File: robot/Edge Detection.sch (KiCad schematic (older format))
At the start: 3 parts

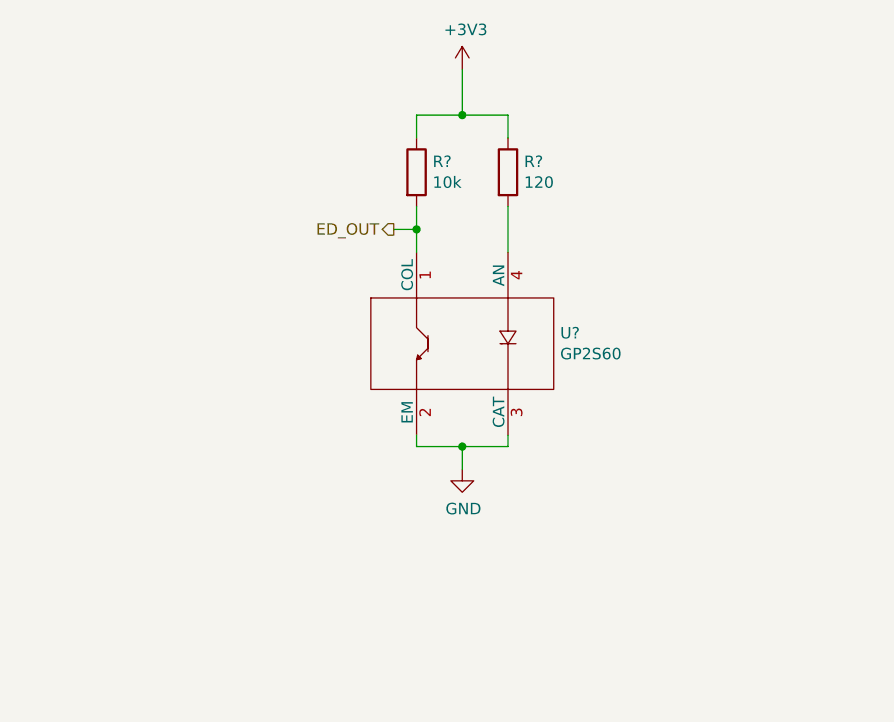
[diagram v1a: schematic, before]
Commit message: UI parts, (re)wiring remaining signals
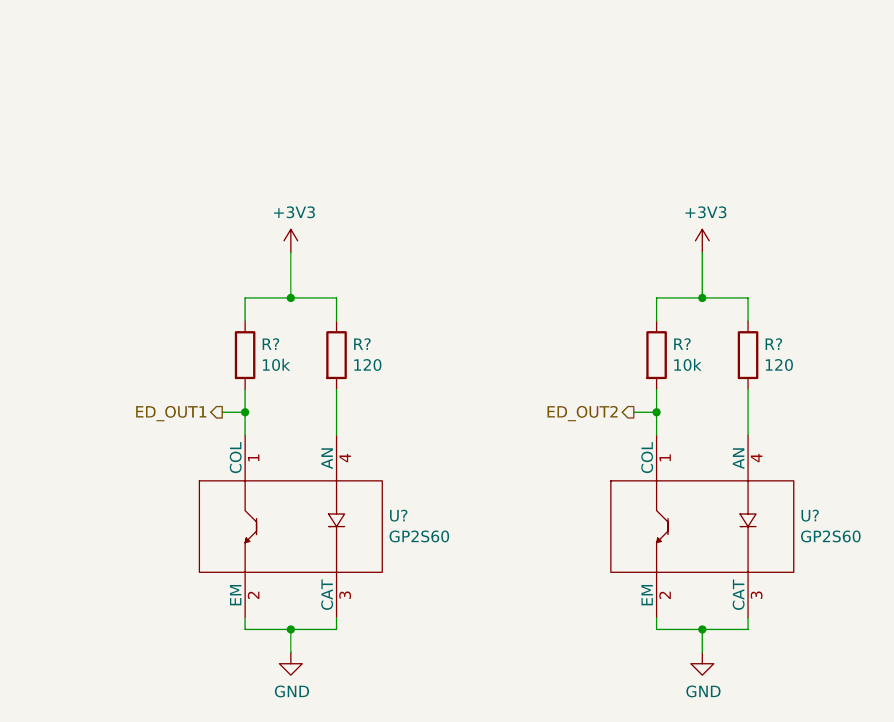
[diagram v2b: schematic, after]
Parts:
- added R?: 120, symbol Device:R
- added R?: 10k, symbol Device:R
- added U?: GP2S60, symbol Custom:GP2S60
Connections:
- net +3V3: now also R?.1, R?.1
- net GND: now also U?.2 (EM), U?.3 (CAT)
- net ED_OUT renamed ED_OUT1
- new net: R?.2, U?.4 (AN)
- new net ED_OUT2: R?.2, U?.1 (COL)
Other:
- moved on the sheet: R?, U?
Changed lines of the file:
@@
 $Descr A4 11693 8268
 encoding utf-8
-Sheet 6 7
+Sheet 5 8
 Title "Edge Detection"
 Date "2019-08-25"
@@
 L Custom:GP2S60 U?
 U 1 1 5D63C480
-P 5800 3600
-F 0 "U?" H 6228 3646 50  0000 L CNN
-F 1 "GP2S60" H 6228 3555 50  0000 L CNN
-F 2 "" H 5800 3600 50  0001 C CNN
-F 3 "" H 5800 3600 50  0001 C CNN
-	1    5800 3600
+P 5050 4400
+F 0 "U?" H 5478 4446 50  0000 L CNN
+F 1 "GP2S60" H 5478 4355 50  0000 L CNN
+F 2 "" H 5050 4400 50  0001 C CNN
+F 3 "" H 5050 4400 50  0001 C CNN
+	1    5050 4400
 	1    0    0    -1
 $EndComp
@@
 L power:GND #PWR0126
 U 1 1 5D63C8BA
-P 5800 4150
-F 0 "#PWR0126" H 5800 3900 50  0001 C CNN
-F 1 "GND" H 5805 3977 50  0000 C CNN
-F 2 "" H 5800 4150 50  0001 C CNN
-F 3 "" H 5800 4150 50  0001 C CNN
-	1    5800 4150
+P 5050 4950
+F 0 "#PWR0126" H 5050 4700 50  0001 C CNN
+F 1 "GND" H 5055 4777 50  0000 C CNN
+F 2 "" H 5050 4950 50  0001 C CNN
+F 3 "" H 5050 4950 50  0001 C CNN
+	1    5050 4950
 	1    0    0    -1
 $EndComp
 Wire Wire Line
-	5600 4000 5600 4050
+	4850 4800 4850 4850
 Wire Wire Line
-	5600 4050 5800 4050
+	4850 4850 5050 4850
 Wire Wire Line
-	5800 4050 5800 4150
+	5050 4850 5050 4950
 Wire Wire Line
-	5800 4050 6000 4050
+	5050 4850 5250 4850
 Wire Wire Line
-	6000 4050 6000 4000
-Connection ~ 5800 4050
-Text HLabel 5500 3100 0    50   Output ~ 0
-ED_OUT
+	5250 4850 5250 4800
+Connection ~ 5050 4850
+Text HLabel 4750 3900 0    50   Output ~ 0
+ED_OUT1
 $Comp
 L Device:R R?
 U 1 1 5D63CB92
-P 6000 2850
-F 0 "R?" H 6070 2896 50  0000 L CNN
-F 1 "120" H 6070 2805 50  0000 L CNN
-F 2 "" V 5930 2850 50  0001 C CNN
-F 3 "~" H 6000 2850 50  0001 C CNN
-	1    6000 2850
+P 5250 3650
+F 0 "R?" H 5320 3696 50  0000 L CNN
+F 1 "120" H 5320 3605 50  0000 L CNN
+F 2 "" V 5180 3650 50  0001 C CNN
+F 3 "~" H 5250 3650 50  0001 C CNN
+	1    5250 3650
 	1    0    0    -1
 $EndComp
@@
 L Device:R R?
 U 1 1 5D63D227
-P 5600 2850
-F 0 "R?" H 5670 2896 50  0000 L CNN
-F 1 "10k" H 5670 2805 50  0000 L CNN
-F 2 "" V 5530 2850 50  0001 C CNN
-F 3 "~" H 5600 2850 50  0001 C CNN
-	1    5600 2850
+P 4850 3650
+F 0 "R?" H 4920 3696 50  0000 L CNN
+F 1 "10k" H 4920 3605 50  0000 L CNN
+F 2 "" V 4780 3650 50  0001 C CNN
+F 3 "~" H 4850 3650 50  0001 C CNN
+	1    4850 3650
 	1    0    0    -1
 $EndComp
 Wire Wire Line
-	5500 3100 5600 3100
+	4750 3900 4850 3900
 Wire Wire Line
-	5600 3100 5600 3000
+	4850 3900 4850 3800
 Wire Wire Line
-	5600 3100 5600 3200
-Connection ~ 5600 3100
+	4850 3900 4850 4000
+Connection ~ 4850 3900
 Wire Wire Line
-	6000 3000 6000 3200
+	5250 3800 5250 4000
 Wire Wire Line
-	5600 2700 5600 2600
+	4850 3500 4850 3400
 Wire Wire Line
-	5600 2600 5800 2600
+	4850 3400 5050 3400
 Wire Wire Line
-	5800 2600 6000 2600
+	5050 3400 5250 3400
 Wire Wire Line
-	6000 2600 6000 2700
-Connection ~ 5800 2600
+	5250 3400 5250 3500
+Connection ~ 5050 3400
 $Comp
 L power:+3V3 #PWR0127
 U 1 1 5D63DB51
-P 5800 2400
-F 0 "#PWR0127" H 5800 2250 50  0001 C CNN
-F 1 "+3V3" H 5815 2573 50  0000 C CNN
-F 2 "" H 5800 2400 50  0001 C CNN
-F 3 "" H 5800 2400 50  0001 C CNN
-	1    5800 2400
+P 5050 3200
+F 0 "#PWR0127" H 5050 3050 50  0001 C CNN
+F 1 "+3V3" H 5065 3373 50  0000 C CNN
+F 2 "" H 5050 3200 50  0001 C CNN
+F 3 "" H 5050 3200 50  0001 C CNN
+	1    5050 3200
 	1    0    0    -1
 $EndComp
 Wire Wire Line
-	5800 2400 5800 2600
+	5050 3200 5050 3400
+$Comp
+L Custom:GP2S60 U?
+U 1 1 5D7195FB
+P 6850 4400
+F 0 "U?" H 7278 4446 50  0000 L CNN
+F 1 "GP2S60" H 7278 4355 50  0000 L CNN
+F 2 "" H 6850 4400 50  0001 C CNN
+F 3 "" H 6850 4400 50  0001 C CNN
+	1    6850 4400
+	1    0    0    -1
+$EndComp
+$Comp
+L power:GND #PWR?
+U 1 1 5D719605
+P 6850 4950
+F 0 "#PWR?" H 6850 4700 50  0001 C CNN
+F 1 "GND" H 6855 4777 50  0000 C CNN
+F 2 "" H 6850 4950 50  0001 C CNN
+F 3 "" H 6850 4950 50  0001 C CNN
+	1    6850 4950
+	1    0    0    -1
+$EndComp
+Wire Wire Line
+	6650 4800 6650 4850
+Wire Wire Line
+	6650 4850 6850 4850
+Wire Wire Line
+	6850 4850 6850 4950
+Wire Wire Line
+	6850 4850 7050 4850
+Wire Wire Line
+	7050 4850 7050 4800
+Connection ~ 6850 4850
+Text HLabel 6550 3900 0    50   Output ~ 0
+ED_OUT2
+$Comp
+L Device:R R?
+U 1 1 5D719616
+P 7050 3650
+F 0 "R?" H 7120 3696 50  0000 L CNN
+F 1 "120" H 7120 3605 50  0000 L CNN
+F 2 "" V 6980 3650 50  0001 C CNN
+F 3 "~" H 7050 3650 50  0001 C CNN
+	1    7050 3650
+	1    0    0    -1
+$EndComp
+$Comp
+L Device:R R?
+U 1 1 5D719620
+P 6650 3650
+F 0 "R?" H 6720 3696 50  0000 L CNN
+F 1 "10k" H 6720 3605 50  0000 L CNN
+F 2 "" V 6580 3650 50  0001 C CNN
+F 3 "~" H 6650 3650 50  0001 C CNN
+	1    6650 3650
+	1    0    0    -1
+$EndComp
+Wire Wire Line
+	6550 3900 6650 3900
+Wire Wire Line
+	6650 3900 6650 3800
+Wire Wire Line
+	6650 3900 6650 4000
+Connection ~ 6650 3900
+Wire Wire Line
+	7050 3800 7050 4000
+Wire Wire Line
+	6650 3500 6650 3400
+Wire Wire Line
+	6650 3400 6850 3400
+Wire Wire Line
+	6850 3400 7050 3400
+Wire Wire Line
+	7050 3400 7050 3500
+Connection ~ 6850 3400
+$Comp
+L power:+3V3 #PWR?
+U 1 1 5D719634
+P 6850 3200
+F 0 "#PWR?" H 6850 3050 50  0001 C CNN
+F 1 "+3V3" H 6865 3373 50  0000 C CNN
+F 2 "" H 6850 3200 50  0001 C CNN
+F 3 "" H 6850 3200 50  0001 C CNN
+	1    6850 3200
+	1    0    0    -1
+$EndComp
+Wire Wire Line
+	6850 3200 6850 3400
 $EndSCHEMATC

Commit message: DRC check fixes and small changes
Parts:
- gave numbers to parts that had none: 6
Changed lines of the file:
@@
 $EndDescr
 $Comp
-L Custom:GP2S60 U?
+L Custom:GP2S60 U5
 U 1 1 5D63C480
 P 5050 4400
-F 0 "U?" H 5478 4446 50  0000 L CNN
+F 0 "U5" H 5478 4446 50  0000 L CNN
 F 1 "GP2S60" H 5478 4355 50  0000 L CNN
 F 2 "" H 5050 4400 50  0001 C CNN
@@
 ED_OUT1
 $Comp
-L Device:R R?
+L Device:R R8
 U 1 1 5D63CB92
 P 5250 3650
-F 0 "R?" H 5320 3696 50  0000 L CNN
+F 0 "R8" H 5320 3696 50  0000 L CNN
 F 1 "120" H 5320 3605 50  0000 L CNN
 F 2 "" V 5180 3650 50  0001 C CNN
@@
 $EndComp
 $Comp
-L Device:R R?
+L Device:R R7
 U 1 1 5D63D227
 P 4850 3650
-F 0 "R?" H 4920 3696 50  0000 L CNN
+F 0 "R7" H 4920 3696 50  0000 L CNN
 F 1 "10k" H 4920 3605 50  0000 L CNN
 F 2 "" V 4780 3650 50  0001 C CNN
@@
 	5050 3200 5050 3400
 $Comp
-L Custom:GP2S60 U?
+L Custom:GP2S60 U6
 U 1 1 5D7195FB
 P 6850 4400
-F 0 "U?" H 7278 4446 50  0000 L CNN
+F 0 "U6" H 7278 4446 50  0000 L CNN
 F 1 "GP2S60" H 7278 4355 50  0000 L CNN
 F 2 "" H 6850 4400 50  0001 C CNN
@@
 $EndComp
 $Comp
-L power:GND #PWR?
+L power:GND #PWR02
 U 1 1 5D719605
 P 6850 4950
-F 0 "#PWR?" H 6850 4700 50  0001 C CNN
+F 0 "#PWR02" H 6850 4700 50  0001 C CNN
 F 1 "GND" H 6855 4777 50  0000 C CNN
 F 2 "" H 6850 4950 50  0001 C CNN
@@
 ED_OUT2
 $Comp
-L Device:R R?
+L Device:R R10
 U 1 1 5D719616
 P 7050 3650
-F 0 "R?" H 7120 3696 50  0000 L CNN
+F 0 "R10" H 7120 3696 50  0000 L CNN
 F 1 "120" H 7120 3605 50  0000 L CNN
 F 2 "" V 6980 3650 50  0001 C CNN
@@
 $EndComp
 $Comp
-L Device:R R?
+L Device:R R9
 U 1 1 5D719620
 P 6650 3650
-F 0 "R?" H 6720 3696 50  0000 L CNN
+F 0 "R9" H 6720 3696 50  0000 L CNN
 F 1 "10k" H 6720 3605 50  0000 L CNN
 F 2 "" V 6580 3650 50  0001 C CNN
@@
 Connection ~ 6850 3400
 $Comp
-L power:+3V3 #PWR?
+L power:+3V3 #PWR01
 U 1 1 5D719634
 P 6850 3200
-F 0 "#PWR?" H 6850 3050 50  0001 C CNN
+F 0 "#PWR01" H 6850 3050 50  0001 C CNN
 F 1 "+3V3" H 6865 3373 50  0000 C CNN
 F 2 "" H 6850 3200 50  0001 C CNN

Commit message: Testpoints, switch, small changes
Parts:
- added TP4, TP5: TestPoint, symbol Connector:TestPoint
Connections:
- net ED_OUT1: now also TP4.1
- net ED_OUT2: now also TP5.1
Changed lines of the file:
@@
 $EndComp
 $Comp
-L power:GND #PWR0126
+L power:GND #PWR028
 U 1 1 5D63C8BA
 P 5050 4950
-F 0 "#PWR0126" H 5050 4700 50  0001 C CNN
+F 0 "#PWR028" H 5050 4700 50  0001 C CNN
 F 1 "GND" H 5055 4777 50  0000 C CNN
 F 2 "" H 5050 4950 50  0001 C CNN
@@
 	5250 4850 5250 4800
 Connection ~ 5050 4850
-Text HLabel 4750 3900 0    50   Output ~ 0
+Text HLabel 4300 3900 0    50   Output ~ 0
 ED_OUT1
 $Comp
@@
 $EndComp
 Wire Wire Line
-	4750 3900 4850 3900
+	4300 3900 4400 3900
 Wire Wire Line
 	4850 3900 4850 3800
@@
 Connection ~ 5050 3400
 $Comp
-L power:+3V3 #PWR0127
+L power:+3V3 #PWR026
 U 1 1 5D63DB51
 P 5050 3200
-F 0 "#PWR0127" H 5050 3050 50  0001 C CNN
+F 0 "#PWR026" H 5050 3050 50  0001 C CNN
 F 1 "+3V3" H 5065 3373 50  0000 C CNN
 F 2 "" H 5050 3200 50  0001 C CNN
@@
 $EndComp
 $Comp
-L power:GND #PWR02
+L power:GND #PWR029
 U 1 1 5D719605
 P 6850 4950
-F 0 "#PWR02" H 6850 4700 50  0001 C CNN
+F 0 "#PWR029" H 6850 4700 50  0001 C CNN
 F 1 "GND" H 6855 4777 50  0000 C CNN
 F 2 "" H 6850 4950 50  0001 C CNN
@@
 	7050 4850 7050 4800
 Connection ~ 6850 4850
-Text HLabel 6550 3900 0    50   Output ~ 0
+Text HLabel 6100 3900 0    50   Output ~ 0
 ED_OUT2
 $Comp
@@
 $EndComp
 Wire Wire Line
-	6550 3900 6650 3900
-Wire Wire Line
 	6650 3900 6650 3800
 Wire Wire Line
@@
 Connection ~ 6850 3400
 $Comp
-L power:+3V3 #PWR01
+L power:+3V3 #PWR027
 U 1 1 5D719634
 P 6850 3200
-F 0 "#PWR01" H 6850 3050 50  0001 C CNN
+F 0 "#PWR027" H 6850 3050 50  0001 C CNN
 F 1 "+3V3" H 6865 3373 50  0000 C CNN
 F 2 "" H 6850 3200 50  0001 C CNN
@@
 Wire Wire Line
 	6850 3200 6850 3400
+$Comp
+L Connector:TestPoint TP4
+U 1 1 5D78614B
+P 4400 3850
+F 0 "TP4" H 4458 3968 50  0000 L CNN
+F 1 "TestPoint" H 4458 3877 50  0000 L CNN
+F 2 "" H 4600 3850 50  0001 C CNN
+F 3 "~" H 4600 3850 50  0001 C CNN
+	1    4400 3850
+	1    0    0    -1
+$EndComp
+$Comp
+L Connector:TestPoint TP5
+U 1 1 5D787562
+P 6200 3850
+F 0 "TP5" H 6258 3968 50  0000 L CNN
+F 1 "TestPoint" H 6258 3877 50  0000 L CNN
+F 2 "" H 6400 3850 50  0001 C CNN
+F 3 "~" H 6400 3850 50  0001 C CNN
+	1    6200 3850
+	1    0    0    -1
+$EndComp
+Wire Wire Line
+	6100 3900 6200 3900
+Wire Wire Line
+	6200 3850 6200 3900
+Connection ~ 6200 3900
+Wire Wire Line
+	6200 3900 6650 3900
+Wire Wire Line
+	4400 3850 4400 3900
+Connection ~ 4400 3900
+Wire Wire Line
+	4400 3900 4850 3900
 $EndSCHEMATC
